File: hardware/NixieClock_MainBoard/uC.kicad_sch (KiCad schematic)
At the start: 10 parts, among them U1 ESP32-WROOM-32E

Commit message: V2.0 release fertig.
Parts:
- added J11: Conn_01x04, Connector_PinHeader_2.54mm:PinHeader_1x04_P2.54mm_Vertical_SMD_Pin1Left, symbol Connector_Generic:Conn_01x04
- added J12: Conn_01x03, Connector_PinHeader_2.54mm:PinHeader_1x03_P2.54mm_Vertical, symbol Connector_Generic:Conn_01x03
- added J13: Conn_01x03, Connector_PinHeader_2.54mm:PinHeader_1x04_P2.54mm_Vertical, symbol Connector_Generic:Conn_01x04
- added R27, R28, R29, R30, R31, R32: 10k, Resistor_SMD:R_0603_1608Metric, symbol Device:R
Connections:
- net WakeUp_1 is gone; now on net CS_2: U1.8 (IO32)
- net +3.3V: now also J12.1 (Pin_1), J13.1 (Pin_1), R27.1, R29.1, R31.1, R32.1
- net CS_0: now also U1.12 (IO27); no longer U1.29 (IO5)
- net CS_2: no longer U1.24 (IO2)
- net CS_MEM_1: now also R31.2
- net EN: now also R29.2, R30.1
- net GND: now also J11.2 (Pin_2), J11.3 (Pin_3), J12.3 (Pin_3), J13.2 (Pin_2)
- net IO0: now also R27.2, R28.1
- net WS28XX: now also U1.9 (IO33); no longer U1.12 (IO27)
- net WakeUp_2: now also U1.7 (IO35), J12.2 (Pin_2); no longer U1.9 (IO33)
- net at U1.14 (IO12): now also R32.2
- net ADC_0: now reaches U1.4 (SENSOR_VP)
- net ADC_0: now also J13.3 (Pin_3)
- net ADC_3: now reaches U1.5 (SENSOR_VN)
- net ADC_3: now also J13.4 (Pin_4)
- new net: J11.4 (Pin_4), R30.2
- new net: J11.1 (Pin_1), R28.2
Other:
- note removed: "Wichtig pinout prüfen. Welche Pins sollten nciht verwendet werden? Einige sind nur Output!!!"
- moved on the sheet: R10, R11, R12, R22, R5, R6, R9

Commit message: Version 2 Ready
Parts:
- R28, R30: value 10k -> 470R
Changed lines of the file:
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@@
 			)
 		)
-		(property "Value" "10k"
+		(property "Value" "470R"
 			(at 236.22 86.3599 0)
 			(effects
@@
 			)
 		)
-		(property "Value" "10k"
+		(property "Value" "470R"
 			(at 256.54 86.3599 0)
 			(effects

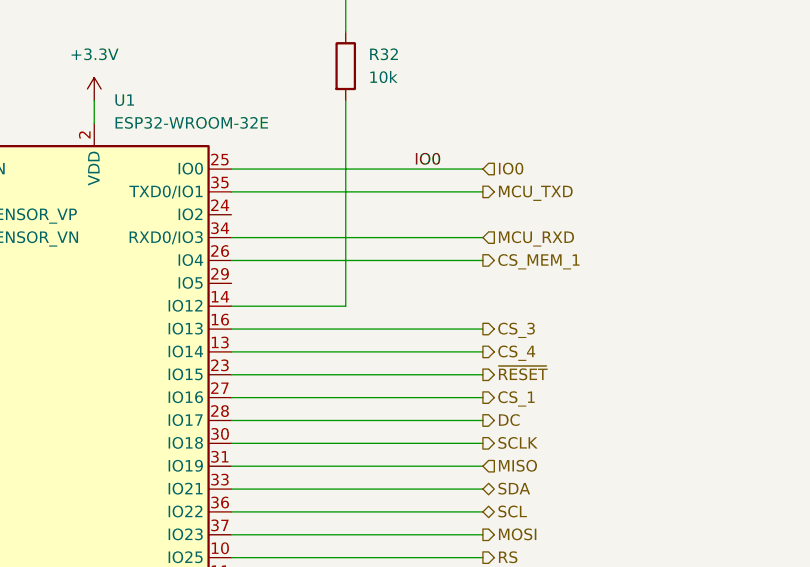
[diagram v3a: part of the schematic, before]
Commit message: Hardware V2.1 add NixieClock_MainBoard/NixieClock_Schematic.pdf
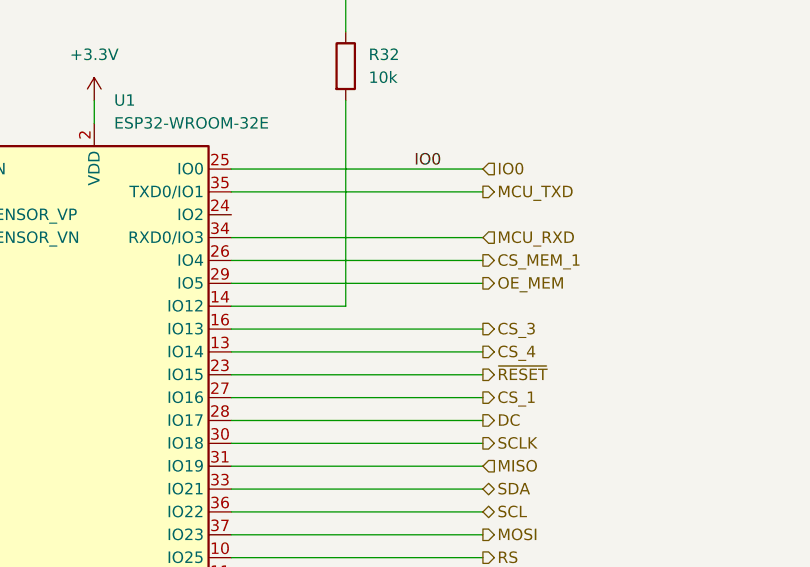
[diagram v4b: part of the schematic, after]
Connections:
- net OE_MEM: now reaches U1.29 (IO5)
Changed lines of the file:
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@@
 (kicad_sch
-	(version 20231120)
+	(version 20250114)
 	(generator "eeschema")
-	(generator_version "8.0")
+	(generator_version "9.0")
 	(paper "A4")
+	(title_block
+		(date "2026-06-07")
+		(rev "2.1")
+	)
 	(junction
 		(at 233.68 78.74)
@@
 	(wire
 		(pts
+			(xy 134.62 100.33) (xy 162.56 100.33)
+		)
+		(stroke
+			(width 0)
+			(type default)
+		)
+	)
+	(wire
+		(pts
 			(xy 134.62 40.64) (xy 134.62 53.34)
 		)
@@
 	(label "CS_4"
 		(at 134.62 48.26 90)
-		(fields_autoplaced yes)
 		(effects
 			(font
@@
 	(label "EN"
 		(at 93.98 87.63 0)
-		(fields_autoplaced yes)
 		(effects
 			(font
@@
 	(label "ADC_3"
 		(at 87.63 95.25 180)
-		(fields_autoplaced yes)
 		(effects
 			(font
@@
 	(label "IO0"
 		(at 243.84 78.74 0)
-		(fields_autoplaced yes)
 		(effects
 			(font
@@
 	(label "CS_1"
 		(at 123.19 48.26 90)
-		(fields_autoplaced yes)
 		(effects
 			(font
@@
 	(label "ADC_0"
 		(at 87.63 92.71 180)
-		(fields_autoplaced yes)
 		(effects
 			(font
@@
 	(label "SDA"
 		(at 151.13 48.26 90)
-		(fields_autoplaced yes)
 		(effects
 			(font
@@
 	(label "EN"
 		(at 223.52 78.74 0)
-		(fields_autoplaced yes)
 		(effects
 			(font
@@
 	(label "CS_2"
 		(at 127 48.26 90)
-		(fields_autoplaced yes)
 		(effects
 			(font
@@
 	(label "WakeUp_2"
 		(at 139.7 152.4 0)
-		(fields_autoplaced yes)
 		(effects
 			(font
@@
 	(label "CS_MEM_1"
 		(at 138.43 52.07 90)
-		(fields_autoplaced yes)
 		(effects
 			(font
@@
 	(label "CS_0"
 		(at 119.38 48.26 90)
-		(fields_autoplaced yes)
 		(effects
 			(font
@@
 	(label "IO0"
 		(at 154.94 87.63 0)
-		(fields_autoplaced yes)
 		(effects
 			(font
@@
 	(label "SCL"
 		(at 154.94 48.26 90)
-		(fields_autoplaced yes)
 		(effects
 			(font
@@
 	(label "CS_3"
 		(at 130.81 48.26 90)
-		(fields_autoplaced yes)
 		(effects
 			(font
@@
 		(shape output)
 		(at 162.56 118.11 0)
-		(fields_autoplaced yes)
 		(effects
 			(font
@@
 		(shape input)
 		(at 162.56 120.65 0)
-		(fields_autoplaced yes)
 		(effects
 			(font
@@
 		(shape output)
 		(at 162.56 97.79 0)
-		(fields_autoplaced yes)
 		(effects
 			(font
@@
 		(shape output)
 		(at 162.56 105.41 0)
-		(fields_autoplaced yes)
 		(effects
 			(font
@@
 		(shape output)
 		(at 162.56 107.95 0)
-		(fields_autoplaced yes)
 		(effects
 			(font
@@
 		(shape input)
 		(at 88.9 87.63 180)
-		(fields_autoplaced yes)
 		(effects
 			(font
@@
 		(shape output)
 		(at 162.56 130.81 0)
-		(fields_autoplaced yes)
 		(effects
 			(font
@@
 		(shape output)
 		(at 162.56 140.97 0)
-		(fields_autoplaced yes)
 		(effects
 			(font
@@
 		(shape input)
 		(at 162.56 95.25 0)
-		(fields_autoplaced yes)
 		(effects
 			(font
@@
 		(shape output)
 		(at 162.56 135.89 0)
-		(fields_autoplaced yes)
 		(effects
 			(font
@@
 		(shape input)
 		(at 162.56 87.63 0)
-		(fields_autoplaced yes)
 		(effects
 			(font
@@
 		(shape output)
 		(at 162.56 110.49 0)
-		(fields_autoplaced yes)
 		(effects
 			(font
@@
 		(shape bidirectional)
 		(at 162.56 125.73 0)
-		(fields_autoplaced yes)
 		(effects
 			(font
@@
 		(shape output)
 		(at 162.56 128.27 0)
-		(fields_autoplaced yes)
 		(effects
 			(font
@@
 		(shape input)
 		(at 162.56 143.51 0)
-		(fields_autoplaced yes)
 		(effects
 			(font
@@
 		(shape output)
 		(at 162.56 133.35 0)
-		(fields_autoplaced yes)
 		(effects
 			(font
@@
 		(shape output)
 		(at 162.56 115.57 0)
-		(fields_autoplaced yes)
 		(effects
 			(font
@@
 		(shape output)
 		(at 162.56 90.17 0)
-		(fields_autoplaced yes)
 		(effects
 			(font
@@
 		(shape bidirectional)
 		(at 162.56 123.19 0)
-		(fields_autoplaced yes)
+		(effects
+			(font
+				(size 1.27 1.27)
+			)
+			(justify left)
+		)
+	)
+	(hierarchical_label "OE_MEM"
+		(shape output)
+		(at 162.56 100.33 0)
 		(effects
 			(font
@@
 		(shape output)
 		(at 162.56 113.03 0)
-		(fields_autoplaced yes)
 		(effects
 			(font
@@
 		(shape output)
 		(at 162.56 138.43 0)
-		(fields_autoplaced yes)
-		(effects
-			(font
+		(effects
+			(font
